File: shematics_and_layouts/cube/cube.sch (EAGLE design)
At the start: 1 part

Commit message: TASK: Basic and ugly cube shematic
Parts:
- added +, -, B+, B-, BH+, BH-, OUT+, OUT-, VIN+, VIN-, VOUT+, VOUT-: MCS08, solpad:MCS08
- added A2: ESP8266, con-lstb:MA04-2
- added C1, C2: 100n, rcl:C-EU050-024X044
- added K1: LD1117AV33, linear:7805T
- added R1: 10K, rcl:R-EU_0207/10
- added R2: 1K, rcl:R-EU_0207/10
- added R3: 2K, rcl:R-EU_0207/10
- added R4: RGP10M, diode:1N4446
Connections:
- new net GND: A1.GND, A1.GND2, A2.7, C1.2, C2.2, K1.GND, R3.2, VOUT-.MP
- new net N$1: OUT+.MP, VIN+.MP
- new net N$2: OUT-.MP, VIN-.MP
- new net N$3: A2.2, C2.1, K1.VO, R1.1, R4.A
- new net N$4: A2.1, R2.2, R3.1
- new net N$5: A2.6, R1.2
- new net N$6: A1.D2, A2.8
- new net N$7: B-.MP, BH-.MP
- new net N$8: A1.D3, R2.1
- new net N$9: B+.MP, BH+.MP
- new net VCC: A1.5.5V, C1.1, K1.VI, R4.C, VOUT+.MP
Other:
- note added: "A1"

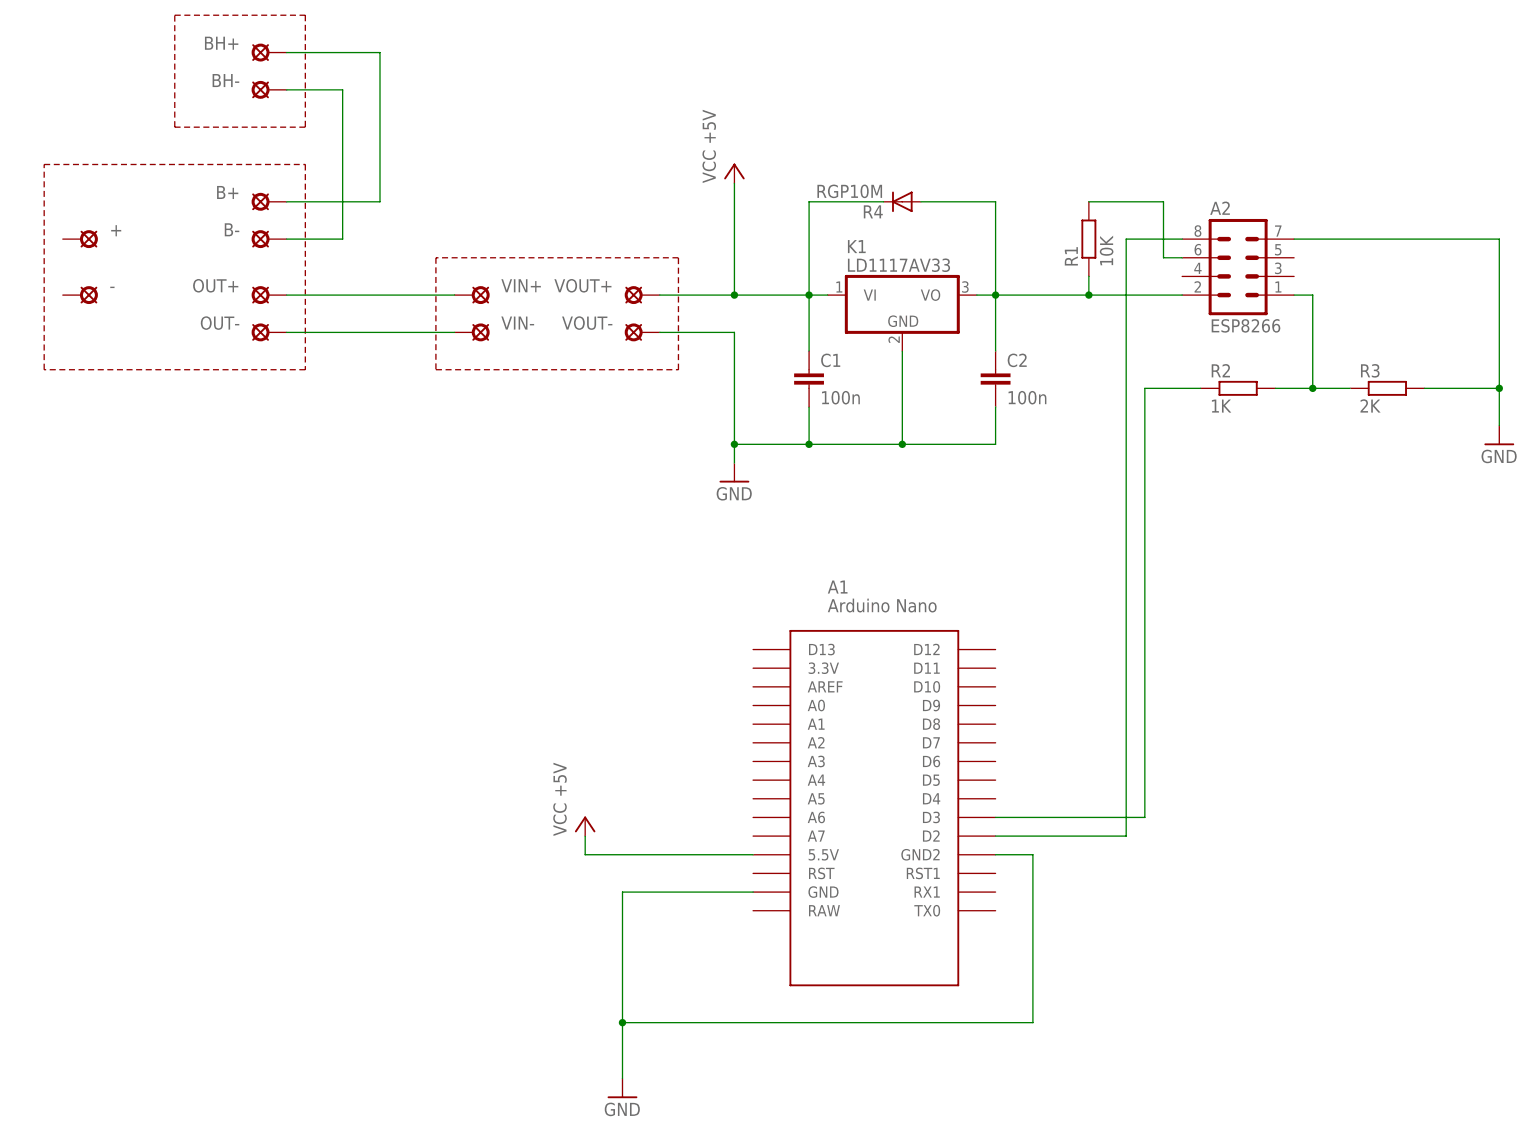
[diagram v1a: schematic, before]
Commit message: TASK: cube shematic and board --> addet all componets, for now
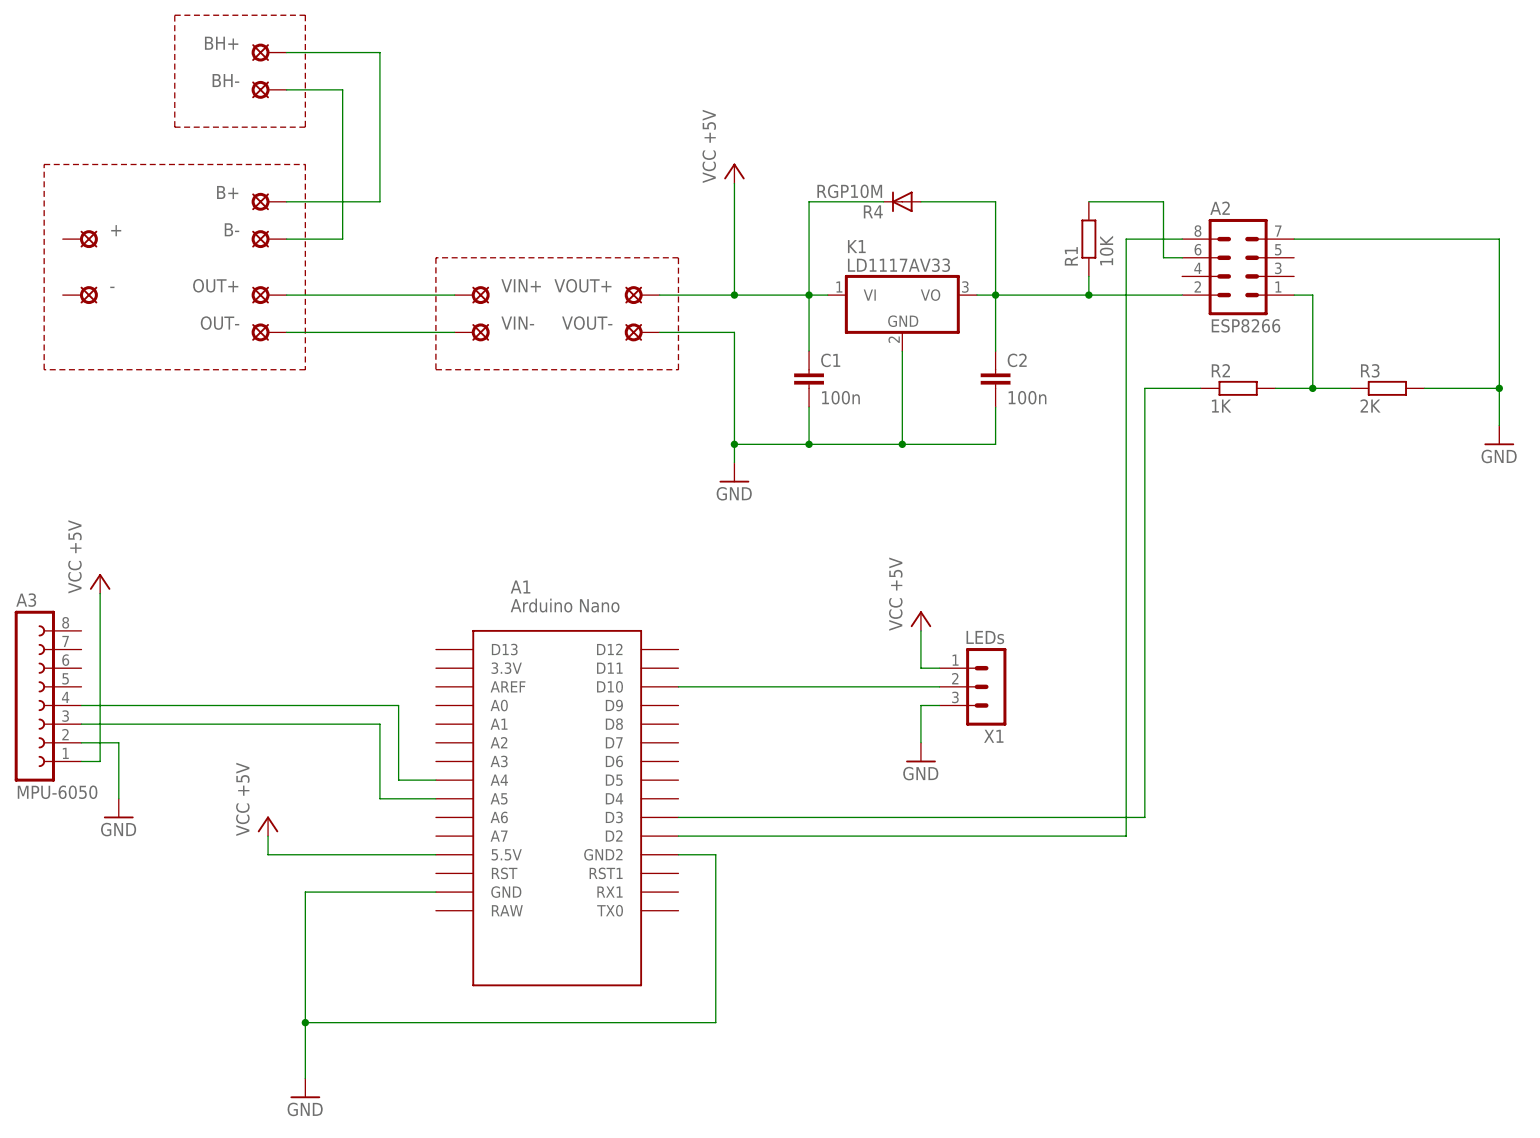
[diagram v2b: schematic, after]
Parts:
- added A3: MPU-6050, con-lsta:FE08-1
- added X1: LEDs, con-lstb:MA03-1
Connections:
- new net N$10: A1.A4, A3.4
- new net N$11: A1.A5, A3.3
- new net N$12: A1.D10, X1.2
- net GND: now also A3.2, X1.3
- net VCC: now also A3.1, X1.1
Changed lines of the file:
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@@
 <part name="BH+" library="solpad" deviceset="MCS08" device=""/>
 <part name="BH-" library="solpad" deviceset="MCS08" device=""/>
+<part name="A3" library="con-lsta" deviceset="FE08-1" device="" value="MPU-6050"/>
+<part name="P+3" library="supply1" deviceset="VCC" device="" value="VCC +5V"/>
+<part name="GND4" library="supply1" deviceset="GND" device=""/>
+<part name="X1" library="con-lstb" deviceset="MA03-1" device="" value="LEDs"/>
+<part name="P+4" library="supply1" deviceset="VCC" device="" value="VCC +5V"/>
+<part name="GND5" library="supply1" deviceset="GND" device=""/>
 </parts>
 <sheets>
@@
 <wire x1="-73.66" y1="142.24" x2="-73.66" y2="157.48" width="0.1524" layer="94" style="dashdot"/>
 <wire x1="-73.66" y1="157.48" x2="-55.88" y2="157.48" width="0.1524" layer="94" style="dashdot"/>
-<text x="15.24" y="78.74" size="1.778" layer="95">A1</text>
+<text x="-27.94" y="78.74" size="1.778" layer="95">A1</text>
 </plain>
 <instances>
-<instance part="A1" gate="G$1" x="27.94" y="55.88" smashed="yes"/>
+<instance part="A1" gate="G$1" x="-15.24" y="55.88" smashed="yes"/>
 <instance part="GND1" gate="1" x="106.68" y="99.06"/>
 <instance part="A2" gate="G$1" x="71.12" y="124.46"/>
@@
 <instance part="GND2" gate="1" x="2.54" y="93.98"/>
 <instance part="P+1" gate="VCC" x="2.54" y="137.16"/>
-<instance part="P+2" gate="VCC" x="-17.78" y="48.26"/>
-<instance part="GND3" gate="1" x="-12.7" y="10.16"/>
+<instance part="P+2" gate="VCC" x="-60.96" y="48.26"/>
+<instance part="GND3" gate="1" x="-55.88" y="10.16"/>
 <instance part="OUT+" gate="G$1" x="-60.96" y="119.38" smashed="yes" rot="R90">
 <attribute name="NAME" x="-64.77" y="121.539" size="1.778" layer="95" rot="R180"/>
@@
 <attribute name="NAME" x="-64.77" y="149.479" size="1.778" layer="95" rot="R180"/>
 </instance>
+<instance part="A3" gate="G$1" x="-93.98" y="63.5"/>
+<instance part="P+3" gate="VCC" x="-83.82" y="81.28"/>
+<instance part="GND4" gate="1" x="-81.28" y="48.26"/>
+<instance part="X1" gate="G$1" x="38.1" y="66.04" rot="R180"/>
+<instance part="P+4" gate="VCC" x="27.94" y="76.2"/>
+<instance part="GND5" gate="1" x="27.94" y="55.88"/>
 </instances>
 <busses>
@@
 <segment>
 <pinref part="GND3" gate="1" pin="GND"/>
-<wire x1="-12.7" y1="12.7" x2="-12.7" y2="20.32" width="0.1524" layer="91"/>
+<wire x1="-55.88" y1="12.7" x2="-55.88" y2="20.32" width="0.1524" layer="91"/>
 <pinref part="A1" gate="G$1" pin="GND"/>
-<wire x1="-12.7" y1="20.32" x2="-12.7" y2="38.1" width="0.1524" layer="91"/>
-<wire x1="-12.7" y1="38.1" x2="5.08" y2="38.1" width="0.1524" layer="91"/>
+<wire x1="-55.88" y1="20.32" x2="-55.88" y2="38.1" width="0.1524" layer="91"/>
+<wire x1="-55.88" y1="38.1" x2="-38.1" y2="38.1" width="0.1524" layer="91"/>
 <pinref part="A1" gate="G$1" pin="GND2"/>
-<wire x1="38.1" y1="43.18" x2="43.18" y2="43.18" width="0.1524" layer="91"/>
-<wire x1="43.18" y1="43.18" x2="43.18" y2="20.32" width="0.1524" layer="91"/>
-<wire x1="43.18" y1="20.32" x2="-12.7" y2="20.32" width="0.1524" layer="91"/>
-<junction x="-12.7" y="20.32"/>
+<wire x1="-5.08" y1="43.18" x2="0" y2="43.18" width="0.1524" layer="91"/>
+<wire x1="0" y1="43.18" x2="0" y2="20.32" width="0.1524" layer="91"/>
+<wire x1="0" y1="20.32" x2="-55.88" y2="20.32" width="0.1524" layer="91"/>
+<junction x="-55.88" y="20.32"/>
+</segment>
+<segment>
+<pinref part="A3" gate="G$1" pin="2"/>
+<wire x1="-86.36" y1="58.42" x2="-81.28" y2="58.42" width="0.1524" layer="91"/>
+<pinref part="GND4" gate="1" pin="GND"/>
+<wire x1="-81.28" y1="58.42" x2="-81.28" y2="50.8" width="0.1524" layer="91"/>
+</segment>
+<segment>
+<pinref part="X1" gate="G$1" pin="3"/>
+<wire x1="30.48" y1="63.5" x2="27.94" y2="63.5" width="0.1524" layer="91"/>
+<pinref part="GND5" gate="1" pin="GND"/>
+<wire x1="27.94" y1="63.5" x2="27.94" y2="58.42" width="0.1524" layer="91"/>
 </segment>
 </net>
@@
 <wire x1="55.88" y1="127" x2="55.88" y2="45.72" width="0.1524" layer="91"/>
 <pinref part="A1" gate="G$1" pin="D2"/>
-<wire x1="38.1" y1="45.72" x2="55.88" y2="45.72" width="0.1524" layer="91"/>
+<wire x1="-5.08" y1="45.72" x2="55.88" y2="45.72" width="0.1524" layer="91"/>
 </segment>
 </net>
@@
 <segment>
 <pinref part="A1" gate="G$1" pin="D3"/>
-<wire x1="38.1" y1="48.26" x2="58.42" y2="48.26" width="0.1524" layer="91"/>
+<wire x1="-5.08" y1="48.26" x2="58.42" y2="48.26" width="0.1524" layer="91"/>
 <wire x1="58.42" y1="48.26" x2="58.42" y2="106.68" width="0.1524" layer="91"/>
 <pinref part="R2" gate="G$1" pin="1"/>
@@
 <segment>
 <pinref part="P+2" gate="VCC" pin="VCC"/>
-<wire x1="-17.78" y1="45.72" x2="-17.78" y2="43.18" width="0.1524" layer="91"/>
+<wire x1="-60.96" y1="45.72" x2="-60.96" y2="43.18" width="0.1524" layer="91"/>
 <pinref part="A1" gate="G$1" pin="5.5V"/>
-<wire x1="-17.78" y1="43.18" x2="5.08" y2="43.18" width="0.1524" layer="91"/>
+<wire x1="-60.96" y1="43.18" x2="-38.1" y2="43.18" width="0.1524" layer="91"/>
+</segment>
+<segment>
+<pinref part="A3" gate="G$1" pin="1"/>
+<wire x1="-86.36" y1="55.88" x2="-83.82" y2="55.88" width="0.1524" layer="91"/>
+<wire x1="-83.82" y1="55.88" x2="-83.82" y2="78.74" width="0.1524" layer="91"/>
+<pinref part="P+3" gate="VCC" pin="VCC"/>
+</segment>
+<segment>
+<pinref part="X1" gate="G$1" pin="1"/>
+<wire x1="30.48" y1="68.58" x2="27.94" y2="68.58" width="0.1524" layer="91"/>
+<pinref part="P+4" gate="VCC" pin="VCC"/>
+<wire x1="27.94" y1="73.66" x2="27.94" y2="68.58" width="0.1524" layer="91"/>
 </segment>
 </net>
@@
 </segment>
 </net>
+<net name="N$10" class="0">
+<segment>
+<pinref part="A1" gate="G$1" pin="A4"/>
+<wire x1="-38.1" y1="53.34" x2="-43.18" y2="53.34" width="0.1524" layer="91"/>
+<wire x1="-43.18" y1="53.34" x2="-43.18" y2="63.5" width="0.1524" layer="91"/>
+<pinref part="A3" gate="G$1" pin="4"/>
+<wire x1="-43.18" y1="63.5" x2="-86.36" y2="63.5" width="0.1524" layer="91"/>
+</segment>
+</net>
+<net name="N$11" class="0">
+<segment>
+<pinref part="A3" gate="G$1" pin="3"/>
+<wire x1="-86.36" y1="60.96" x2="-45.72" y2="60.96" width="0.1524" layer="91"/>
+<wire x1="-45.72" y1="60.96" x2="-45.72" y2="50.8" width="0.1524" layer="91"/>
+<pinref part="A1" gate="G$1" pin="A5"/>
+<wire x1="-45.72" y1="50.8" x2="-38.1" y2="50.8" width="0.1524" layer="91"/>
+</segment>
+</net>
+<net name="N$12" class="0">
+<segment>
+<pinref part="A1" gate="G$1" pin="D10"/>
+<pinref part="X1" gate="G$1" pin="2"/>
+<wire x1="-5.08" y1="66.04" x2="30.48" y2="66.04" width="0.1524" layer="91"/>
+</segment>
+</net>
